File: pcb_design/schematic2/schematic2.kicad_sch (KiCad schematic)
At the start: 29 parts, among them J1 GND | Vcc, J2 I+ | I- | O+ | O- | B+ | B-, J3 R | CC | G | B, SW1 A Button, SW2 B Button, SW3 DPAD UP, SW4 DPAD DOWN, SW5 DPAD LEFT, SW6 DPAD RIGHT, SW7 Opt Button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

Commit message: Update schematic2.kicad_sch file
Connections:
- net at U1.16 (GPIO10/ADC1_CH9): now also R11.2, R12.1
- now unconnected: U1.31 (GPIO0)
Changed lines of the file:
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@@
   (no_connect (at 97.79 95.25))
   (no_connect (at 148.59 146.05))
+  (no_connect (at 148.59 90.17))
   (no_connect (at 97.79 82.55))
   (no_connect (at 148.59 151.13))
@@
   (no_connect (at 148.59 133.35))
   (no_connect (at 148.59 120.65))
-  (no_connect (at 148.59 115.57))
   (no_connect (at 148.59 80.01))
   (wire (pts (xy 180.34 175.26) (xy 85.09 175.26))
@@
     (stroke (width 0) (type default))
   )
-  (wire (pts (xy 194.31 57.15) (xy 194.31 49.53))
+  (wire (pts (xy 194.31 50.8) (xy 194.31 49.53))
     (stroke (width 0) (type default))
   )
@@
     (stroke (width 0) (type default))
   )
-  (wire (pts (xy 172.72 90.17) (xy 172.72 57.15))
+  (wire (pts (xy 171.45 50.8) (xy 171.45 115.57))
     (stroke (width 0) (type default))
   )
@@
     (stroke (width 0) (type default))
   )
+  (wire (pts (xy 148.59 92.71) (xy 182.88 92.71))
+    (stroke (width 0) (type default))
+  )
   (wire (pts (xy 189.23 44.45) (xy 210.82 44.45))
     (stroke (width 0) (type default) (color 255 0 0 1))
@@
     (stroke (width 0) (type default))
   )
-  (wire (pts (xy 172.72 57.15) (xy 194.31 57.15))
+  (wire (pts (xy 171.45 50.8) (xy 194.31 50.8))
     (stroke (width 0) (type default))
   )
@@
     (stroke (width 0) (type default) (color 0 0 0 1))
   )
+  (wire (pts (xy 148.59 115.57) (xy 171.45 115.57))
+    (stroke (width 0) (type default))
+  )
   (wire (pts (xy 130.81 49.53) (xy 154.94 49.53))
     (stroke (width 0) (type default) (color 255 0 0 1))
@@
     (stroke (width 0) (type default))
   )
-  (wire (pts (xy 148.59 92.71) (xy 182.88 92.71))
-    (stroke (width 0) (type default))
-  )
   (wire (pts (xy 154.94 49.53) (xy 154.94 52.07))
     (stroke (width 0) (type default) (color 255 0 0 1))
@@
     (stroke (width 0) (type default) (color 255 0 0 1))
   )
-  (wire (pts (xy 148.59 90.17) (xy 172.72 90.17))
-    (stroke (width 0) (type default))
-  )
   (wire (pts (xy 179.07 173.99) (xy 86.36 173.99))

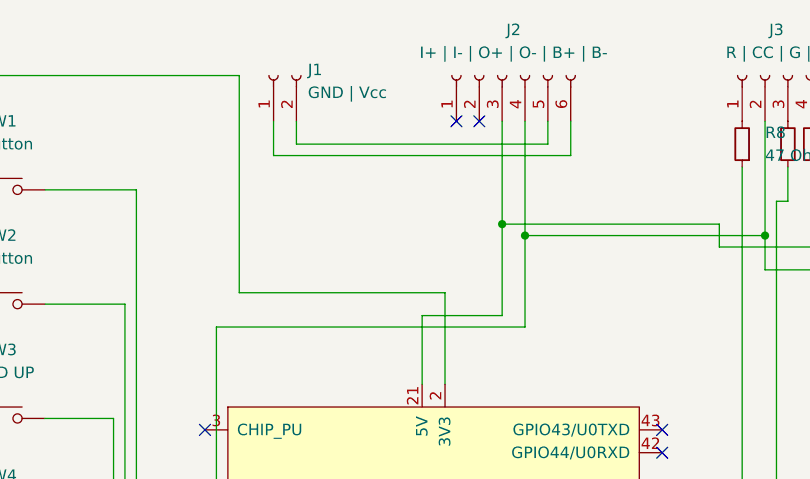
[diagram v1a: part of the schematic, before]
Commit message: Added switch to PCB design and fixed battery readings
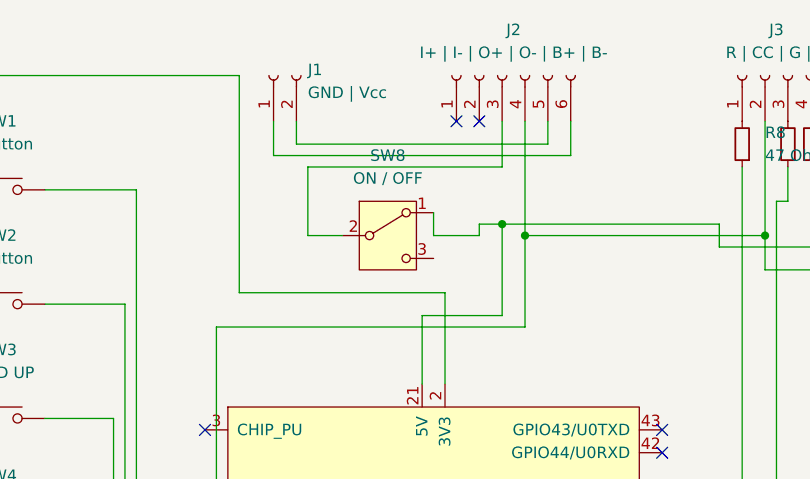
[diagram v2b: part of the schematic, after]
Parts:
- added SW8: ON / OFF, Connector_PinSocket_2.54mm:PinSocket_1x03_P2.54mm_Vertical, symbol Switch:SW_SPDT
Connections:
- net at R11.1, U1.21 (5V): now also SW8.1 (A); no longer J2.3 (Pin_3)
- new net: J2.3 (Pin_3), SW8.2 (B)
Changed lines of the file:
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@@
   (junction (at 59.69 114.3) (diameter 0) (color 0 0 0 0)
   )
+  (junction (at 130.81 49.53) (diameter 0) (color 0 0 0 0)
+  )
   (junction (at 59.69 85.09) (diameter 0) (color 0 0 0 0)
   )
@@
   )
   (junction (at 133.35 50.8) (diameter 0) (color 0 0 0 0)
-  )
-  (junction (at 130.81 49.53) (diameter 0) (color 0 0 0 0)
   )
   (junction (at 219.71 44.45) (diameter 0) (color 0 0 0 0)
@@
     (stroke (width 0) (type default))
   )
+  (wire (pts (xy 128.27 49.53) (xy 128.27 50.8))
+    (stroke (width 0) (type default) (color 255 0 0 1))
+  )
   (wire (pts (xy 59.69 71.12) (xy 59.69 85.09))
     (stroke (width 0) (type default) (color 255 0 0 1))
@@
     (stroke (width 0) (type default))
   )
+  (wire (pts (xy 109.22 50.8) (xy 109.22 43.18))
+    (stroke (width 0) (type default) (color 255 0 0 1))
+  )
   (wire (pts (xy 181.61 95.25) (xy 181.61 176.53))
     (stroke (width 0) (type default))
@@
     (stroke (width 0) (type default) (color 255 0 0 1))
   )
+  (wire (pts (xy 113.03 50.8) (xy 109.22 50.8))
+    (stroke (width 0) (type default) (color 255 0 0 1))
+  )
   (wire (pts (xy 99.06 158.75) (xy 99.06 60.96))
     (stroke (width 0) (type default) (color 0 0 0 1))
@@
     (stroke (width 0) (type default))
   )
+  (wire (pts (xy 109.22 43.18) (xy 130.81 43.18))
+    (stroke (width 0) (type default) (color 255 0 0 1))
+  )
   (wire (pts (xy 171.45 50.8) (xy 194.31 50.8))
     (stroke (width 0) (type default))
   )
-  (wire (pts (xy 130.81 38.1) (xy 130.81 49.53))
+  (wire (pts (xy 130.81 49.53) (xy 128.27 49.53))
     (stroke (width 0) (type default) (color 255 0 0 1))
   )
@@
     (stroke (width 0) (type default))
   )
+  (wire (pts (xy 123.19 48.26) (xy 123.19 50.8))
+    (stroke (width 0) (type default) (color 255 0 0 1))
+  )
   (wire (pts (xy 88.9 171.45) (xy 176.53 171.45))
     (stroke (width 0) (type default))
@@
     (stroke (width 0) (type default) (color 255 0 0 1))
   )
+  (wire (pts (xy 130.81 43.18) (xy 130.81 38.1))
+    (stroke (width 0) (type default) (color 255 0 0 1))
+  )
   (wire (pts (xy 162.56 46.99) (xy 162.56 43.18))
     (stroke (width 0) (type default))
@@
   (wire (pts (xy 88.9 58.42) (xy 80.01 58.42))
     (stroke (width 0) (type default))
+  )
+  (wire (pts (xy 128.27 50.8) (xy 123.19 50.8))
+    (stroke (width 0) (type default) (color 255 0 0 1))
   )
   (wire (pts (xy 82.55 129.54) (xy 82.55 177.8))
@@
         )
       )
+    )
+  )
+  (symbol (lib_id "Switch:SW_SPDT") (at 118.11 50.8 0) (unit 1)
+    (in_bom yes) (on_board yes) (dnp no) (fields_autoplaced)
+    (property "Reference" "SW8" (at 118.11 41.91 0)
+      (effects (font (size 1.27 1.27)))
+    )
+    (property "Value" "ON / OFF" (at 118.11 44.45 0)
+      (effects (font (size 1.27 1.27)))
+    )
+    (property "Footprint" "Connector_PinSocket_2.54mm:PinSocket_1x03_P2.54mm_Vertical" (at 118.11 50.8 0)
+      (effects (font (size 1.27 1.27)) hide)
+    )
+    (property "Datasheet" "~" (at 118.11 58.42 0)
+      (effects (font (size 1.27 1.27)) hide)
+    )
+    (pin "3")
+    (pin "1")
+    (pin "2")
+    (instances
+      (project "schematic2"
+        (path "/fc16f38e-f029-4440-a219-d5ae63df11c7"
+          (reference "SW8") (unit 1)
+        )
+      )

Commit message: kicad files
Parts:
- removed H5, H6: MountingHole, MountingHole:MountingHole_2.5mm_Pad, symbol Mechanical:MountingHole
- added J4: +3.3 LEFT, MountingHole:MountingHole_2.5mm_Pad, symbol Connector:Conn_01x01_Socket
- added J5: +3.3 RIGHT, MountingHole:MountingHole_2.5mm_Pad, symbol Connector:Conn_01x01_Socket
- U1: footprint PCM_Espressif:ESP32-S3-DevKitC -> PCM_Espressif:ESP32S3_Dev_Module
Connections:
- net at R1.1, R2.1, R3.1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: now also J4.1 (Pin_1), J5.1 (Pin_1)
- net at SW6.2: now also U1.30 (GPIO45); no longer U1.40 (GPIO2/ADC1_CH1)
- net at J1.1 (Pin_1), J2.6 (Pin_6): now also J2.4 (Pin_4), J3.2 (Pin_2), R12.2, U1.22 (GND), U1.23 (GND), U1.24 (GND), U1.44 (GND)
- net at SW7.2: now also U1.4 (GPIO4/ADC1_CH3); no longer U1.41 (GPIO1/ADC1_CH0)
- net at SW3.2: now also U1.27 (GPIO21); no longer U1.5 (GPIO5/ADC1_CH4)
- net at U1.13 (GPIO3/ADC1_CH2): no longer SW5.2
- net at R11.2, R12.1: now also U1.5 (GPIO5/ADC1_CH4); no longer U1.16 (GPIO10/ADC1_CH9)
- net at U1.35 (GPIO38): now also SW5.2
- net at U1.39 (GPIO42/MTMS): now also SW4.2
- no-connect marks 28 -> 29
